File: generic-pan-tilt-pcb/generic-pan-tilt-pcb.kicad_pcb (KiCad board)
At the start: 2 copper layers, 104 x 57 mm, 85 parts, among them J1 B4P-VH-FB-B, J10 USB4105-GF-A, J11 Conn_01x08, J12 Conn_01x08, J13 Conn_01x05, J2 NC5MAV, J3 NC5FAV, J5 BM03B-SRSS-TBT, J7 BM03B-SRSS-TBT, J8 B12B-PH-SM4-TBT, J9 B12B-PH-SM4-TBT, SW1 PTS 647 SK70 SMTR2 LFS, SW2 PTS 647 SK70 SMTR2 LFS, SW3 219-12LPST, U1 RP2040, U2 W25Q128JVS, U3 AP63203WU, U4 ISO1450DW, U5 MCP23017_SO, U6 LIS3DH, Y1 ABM8-272-T3

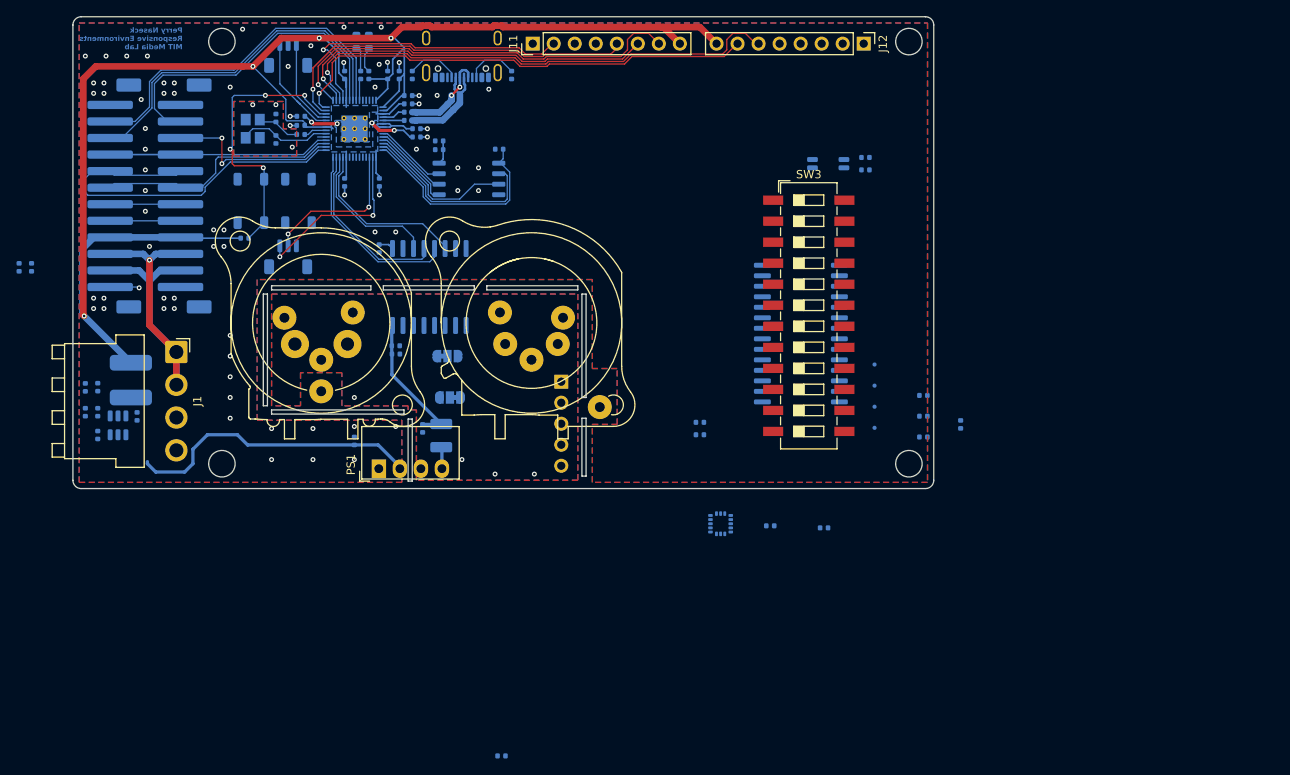
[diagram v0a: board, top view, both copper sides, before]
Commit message: finish rp2040 layout
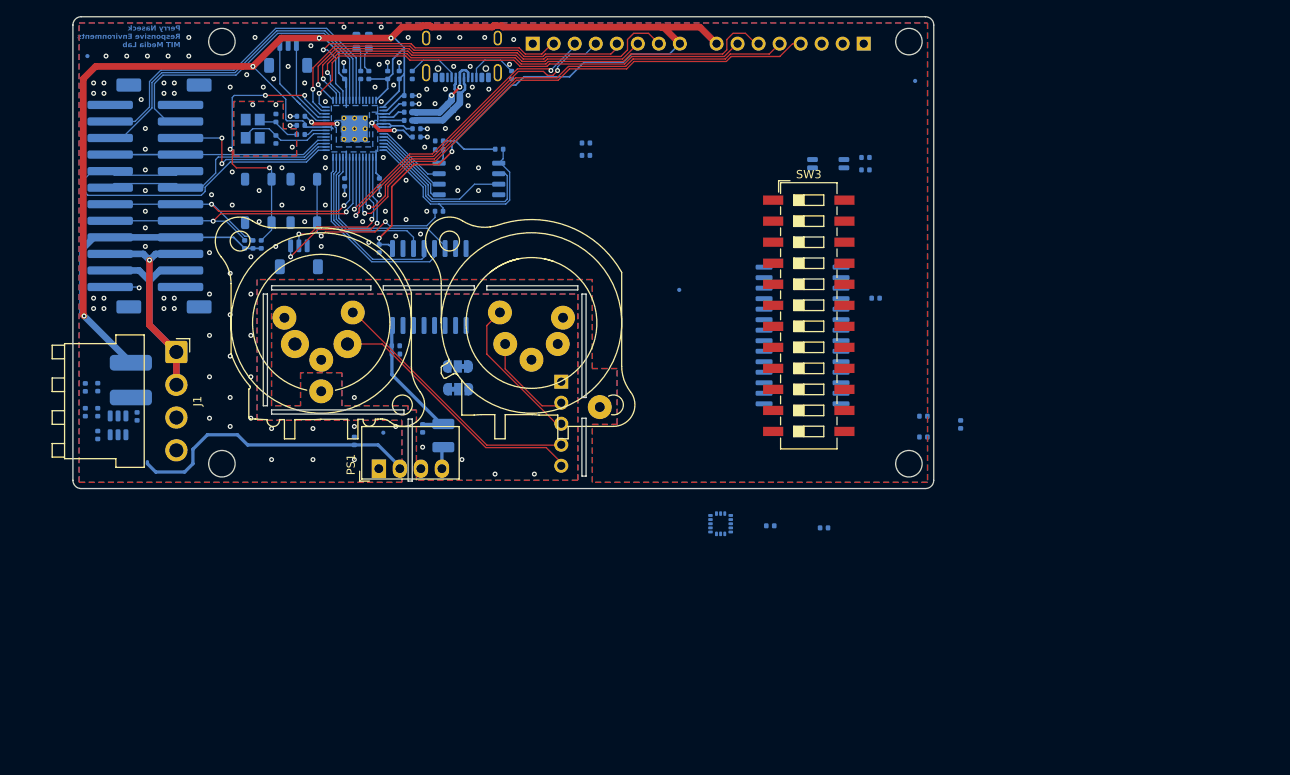
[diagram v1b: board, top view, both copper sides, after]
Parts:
- J11, J12: footprint Connector_PinHeader_2.54mm:PinHeader_1x08_P2.54mm_Vertical -> Connector_PinSocket_2.54mm:PinSocket_1x08_P2.54mm_Vertical; moved to B.Cu
- J13: footprint Connector_PinHeader_2.54mm:PinHeader_1x05_P2.54mm_Vertical -> Connector_PinSocket_2.54mm:PinSocket_1x05_P2.54mm_Vertical
- moved FID1 102.1 mm to (82.8, 71.2)
- moved R2 66.2 mm to (125.2, 90.0)
- moved FID3 59.4 mm to (118.5, 116.8)
- moved FID2 37.1 mm to (182.8, 74.2)
- moved R11 36.5 mm to (143.0, 83.2)
- moved R12 36.5 mm to (143.0, 81.8)
- moved FID4 28.9 mm to (154.2, 99.5)
- moved R14 28.4 mm to (102.8, 94.0)
- moved R13 25.9 mm to (101.8, 94.0)
- moved R15 13.1 mm to (178.0, 100.5)
- moved JP2 4.21 mm to (127.5, 111.5)
- moved JP1 3.87 mm to (127.5, 108.8)
- moved R8 2.14 mm to (103.8, 94.0), turned to 90 degrees
- moved J7 1.30 mm to (108.3, 95.5)
- moved SW2 0.90 mm to (103.4, 88.8)
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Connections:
- J13 pad 2: /generic-pan-tilt-pcb_dmx-expansion/EXP_OUT_+ -> /generic-pan-tilt-pcb_dmx-expansion/EXP_OUT_-
- J13 pad 3: /generic-pan-tilt-pcb_dmx-expansion/EXP_OUT_- -> /generic-pan-tilt-pcb_dmx-expansion/EXP_OUT_+
- J13 pad 4: /generic-pan-tilt-pcb_dmx-expansion/EXP_IN_- -> /generic-pan-tilt-pcb_dmx-expansion/EXP_IN_+
- J13 pad 5: /generic-pan-tilt-pcb_dmx-expansion/EXP_IN_+ -> /generic-pan-tilt-pcb_dmx-expansion/EXP_IN_-
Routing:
- net /EXP_IRQ1: track 0.00 -> 68.8 mm, vias 0 -> 1
- net /EXP_IRQ0: track 0.00 -> 64.7 mm, vias 0 -> 1
- net +3V3: track 256.5 -> 316.3 mm, vias 4 -> 6
- net /I2C0_SDA: track 0.00 -> 46.5 mm, vias 0 -> 2
- net /I2C0_SCL: track 0.00 -> 41.7 mm, vias 0 -> 2
- net /I2C_MOT_SCL: track 8.50 -> 41.8 mm, vias 0 -> 2
- net /I2C_MOT_SDA: track 8.50 -> 40.8 mm, vias 0 -> 2
- net /generic-pan-tilt-pcb_dmx-expansion/EXP_IN_-: track 0.00 -> 32.1 mm
- net /generic-pan-tilt-pcb_dmx-expansion/EXP_IN_+: track 0.00 -> 31.8 mm
- net Net-(R2-Pad2): track 0.00 -> 22.9 mm, vias 0 -> 2
- net /generic-pan-tilt-pcb_dmx-expansion/EXP_OUT_+: track 0.00 -> 18.2 mm
- net /generic-pan-tilt-pcb_dmx-expansion/EXP_OUT_-: track 0.00 -> 11.8 mm
- net /RS485_RX: track 17.7 -> 19.3 mm
- net /RS485_TX: track 20.5 -> 22.1 mm
- net /BOOTSEL: track 26.2 -> 27.3 mm
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
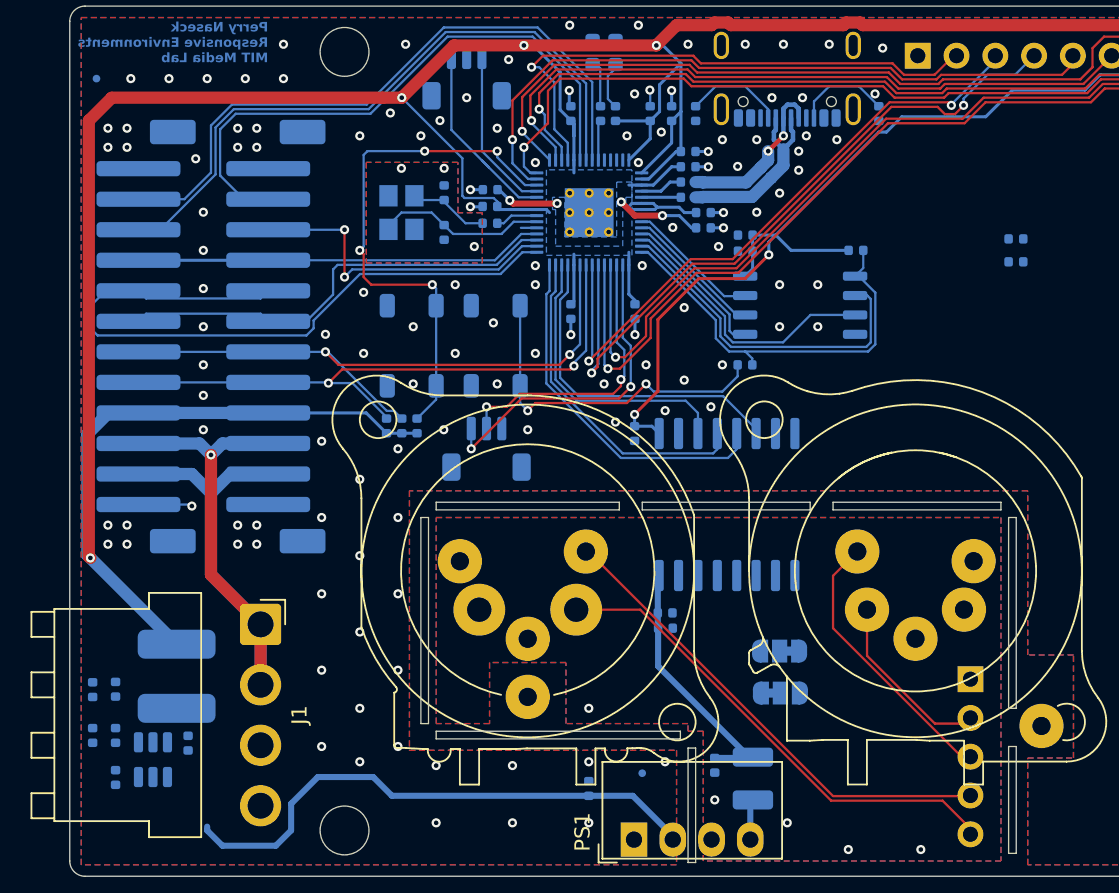
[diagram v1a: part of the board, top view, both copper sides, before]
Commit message: route rs485
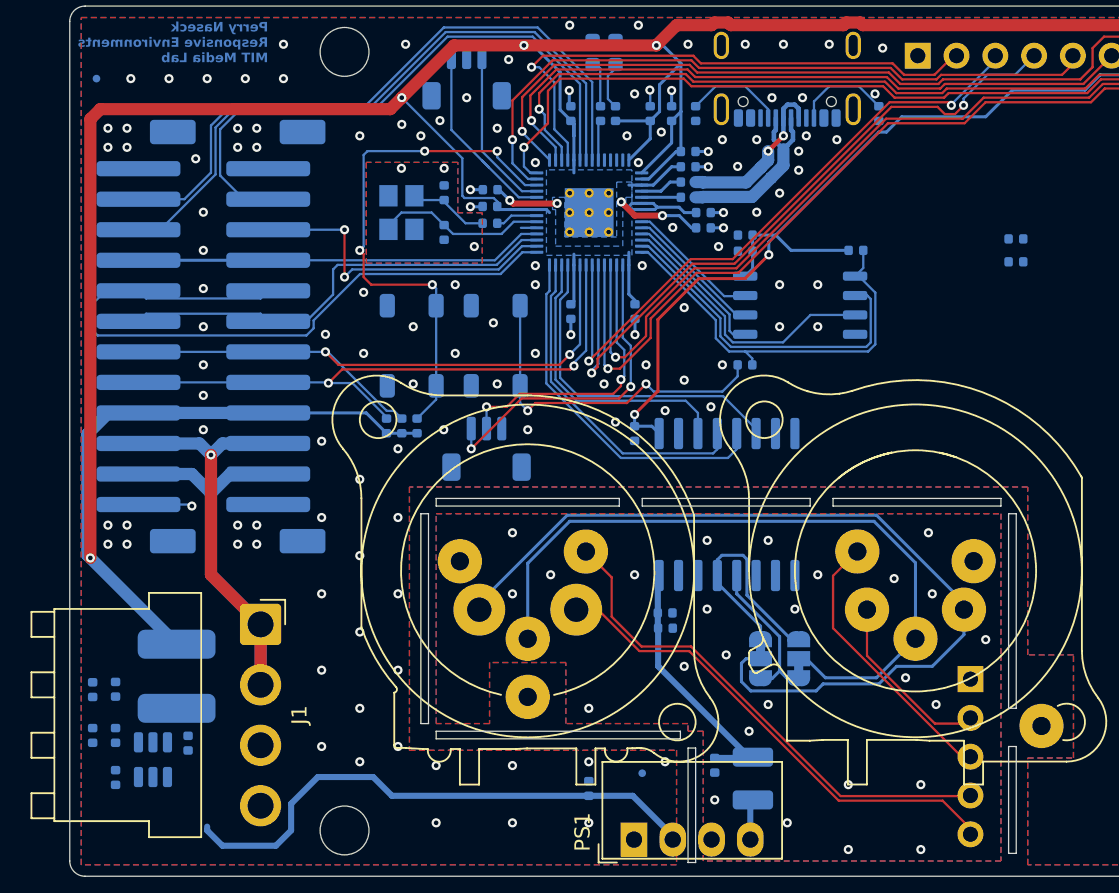
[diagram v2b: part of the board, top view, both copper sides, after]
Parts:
- moved JP2 2.60 mm to (126.2, 109.2), turned to -90 degrees
- moved JP1 1.35 mm to (128.8, 109.2), turned to 90 degrees
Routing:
- net /RS485_B-: track 0.00 -> 58.0 mm
- net /RS485_A+: track 0.00 -> 46.8 mm
- net /RS485_OUT_B-: track 0.00 -> 15.7 mm
- net /RS485_OUT_A+: track 0.00 -> 10.3 mm
- net /generic-pan-tilt-pcb_dmx-expansion/EXP_IN_+: track 31.8 -> 33.4 mm
- net /RS485_GND: vias 5 -> 26
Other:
- outline, holes or cut-outs redrawn

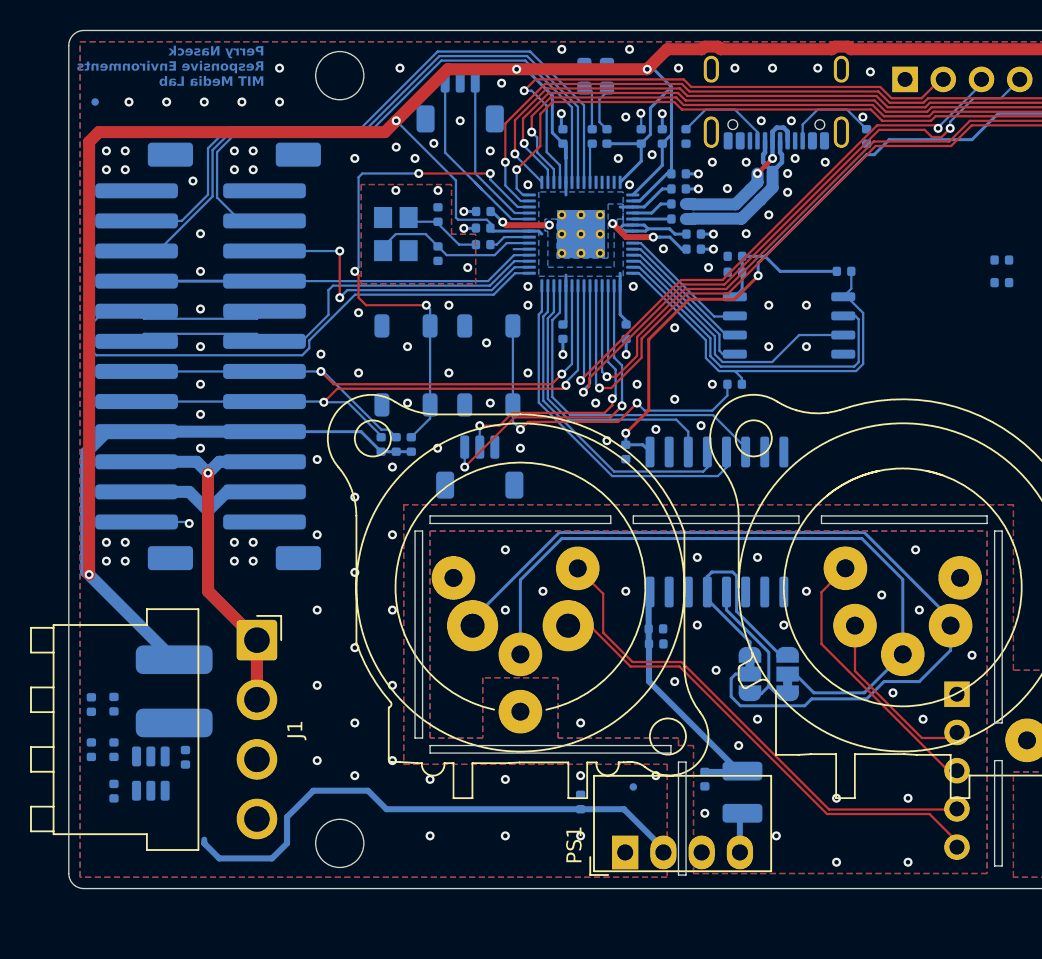
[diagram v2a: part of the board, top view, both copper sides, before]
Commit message: route 3v3 reg, move vh connector
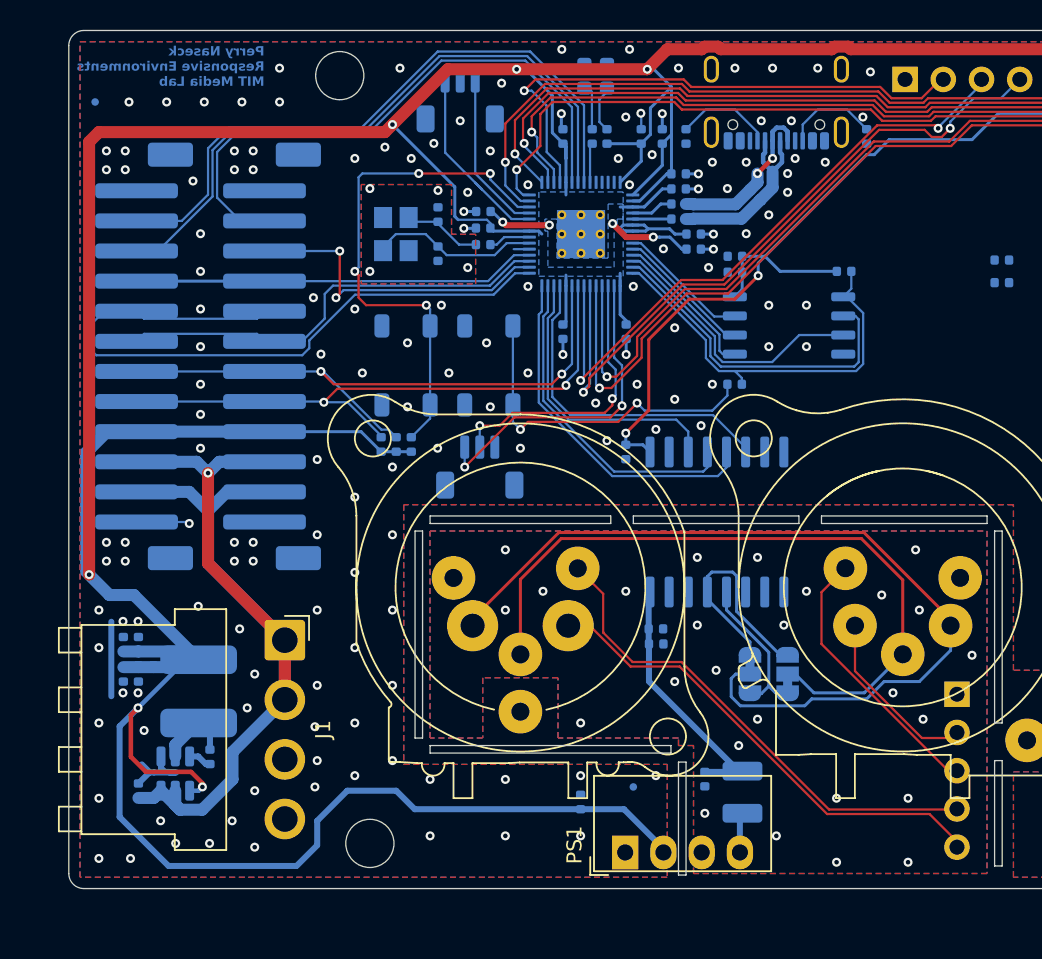
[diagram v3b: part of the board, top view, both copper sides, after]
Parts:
- moved C20 5.44 mm to (84.6, 109.3)
- moved C19 5.26 mm to (85.6, 109.3)
- moved C22 4.53 mm to (84.6, 107.3)
- moved C21 4.30 mm to (85.6, 107.3)
- moved H4 2.00 mm to (101.0, 120.5)
- moved J1 1.85 mm to (95.3, 107.0)
- moved C17 1.63 mm to (85.6, 117.0)
- moved C18 1.63 mm to (90.4, 114.8)
- moved L1 1.62 mm to (89.6, 110.4)
- moved U3 1.62 mm to (88.1, 115.9)
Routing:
- net +3V3: track 316.2 -> 357.7 mm, vias 6 -> 8
- net +24V: track 49.0 -> 67.2 mm
- net GND: track 14.8 -> 25.2 mm, vias 128 -> 153
- net /generic-pan-tilt-pcb_24v_to_3.3v/+3V3_UNFILTERED: track 0.00 -> 5.01 mm
- net /generic-pan-tilt-pcb_24v_to_3.3v/+3V3_BST: track 0.00 -> 1.56 mm

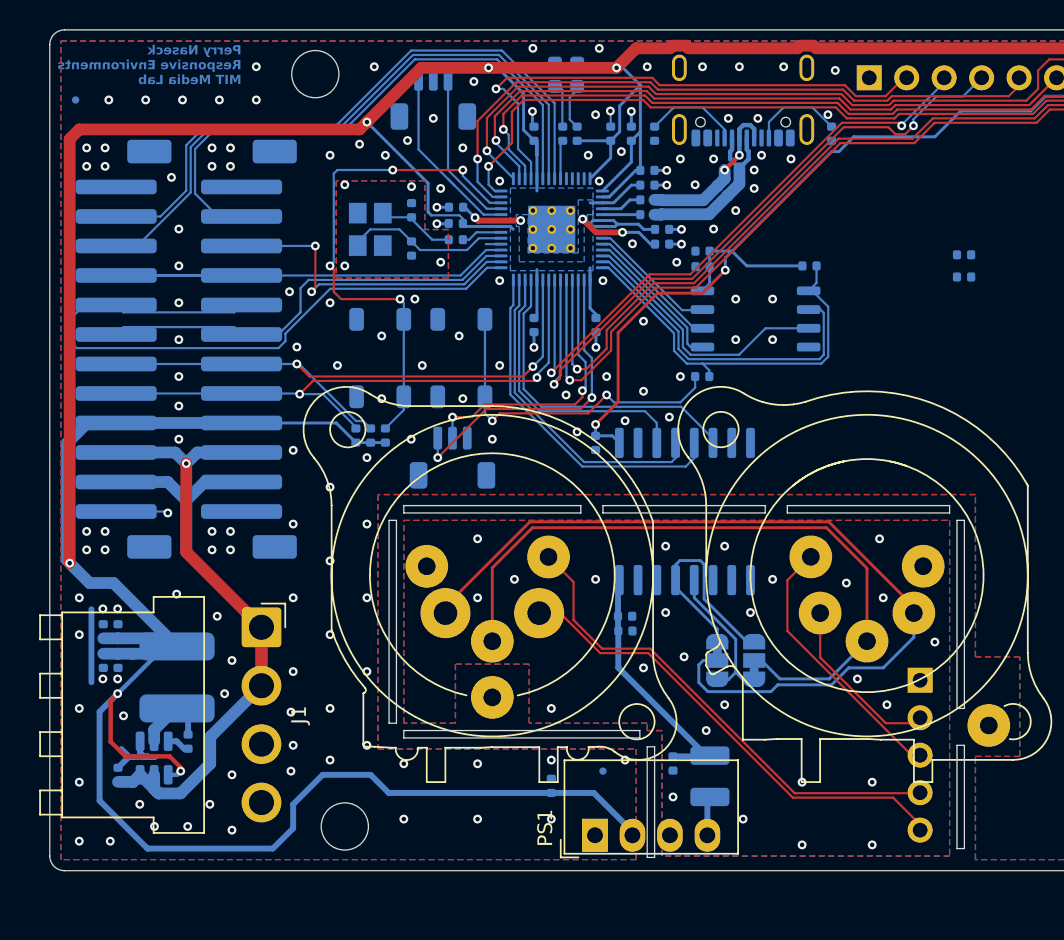
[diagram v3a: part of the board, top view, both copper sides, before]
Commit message: rotate vh connector, stitch rs485
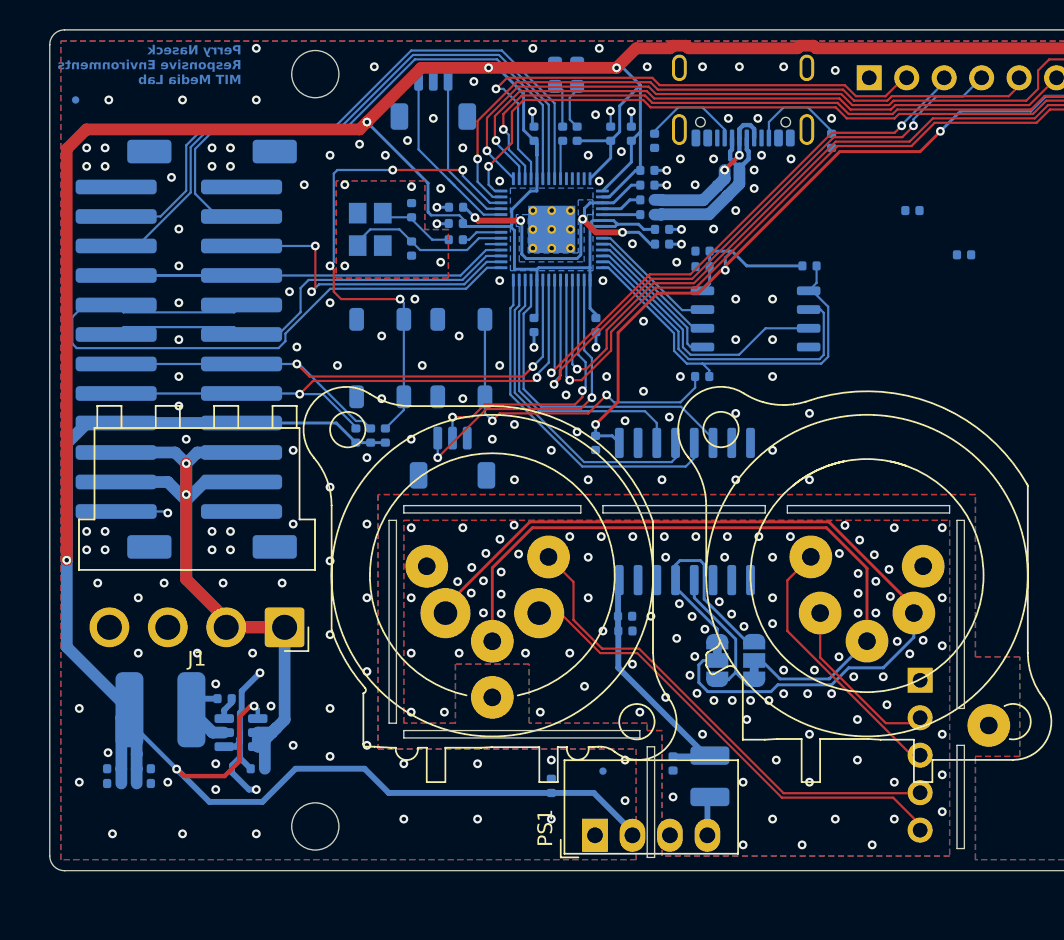
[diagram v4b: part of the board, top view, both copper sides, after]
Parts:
- moved C22 10.3 mm to (85.4, 117.6), turned to 180 degrees
- moved C17 9.48 mm to (95.1, 116.6), turned to 180 degrees
- moved C21 9.32 mm to (85.4, 116.6), turned to 180 degrees
- moved C20 8.76 mm to (87.4, 117.6), turned to 0 degrees
- moved C19 7.52 mm to (87.4, 116.6), turned to 0 degrees
- moved U3 6.14 mm to (94.0, 114.1), turned to 180 degrees
- moved R11 5.70 mm to (139.5, 78.8)
- moved C18 3.82 mm to (92.8, 111.8), turned to 180 degrees
- moved L1 2.46 mm to (88.5, 112.6), turned to 180 degrees
- moved H4 2.00 mm to (99.0, 120.5)
- moved J1 1.57 mm to (96.9, 107.0), turned to 180 degrees
- moved R4 0.48 mm to (134.0, 74.0)
- moved R5 0.48 mm to (122.0, 74.0)
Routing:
- net +1V1: track 17.0 -> 27.3 mm
- net +24V: track 67.2 -> 64.8 mm, vias 1 -> 2
- net +3V3: track 357.7 -> 360.0 mm, vias 8 -> 9
- net GND: track 25.2 -> 27.4 mm, vias 153 -> 160
- net /RS485_GND: vias 26 -> 103
